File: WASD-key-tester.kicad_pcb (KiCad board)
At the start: 2 copper layers, 117 x 20 mm, 26 parts, among them J1 USB_B, J2 Conn_01x06, U1 ATTINY85-20SU

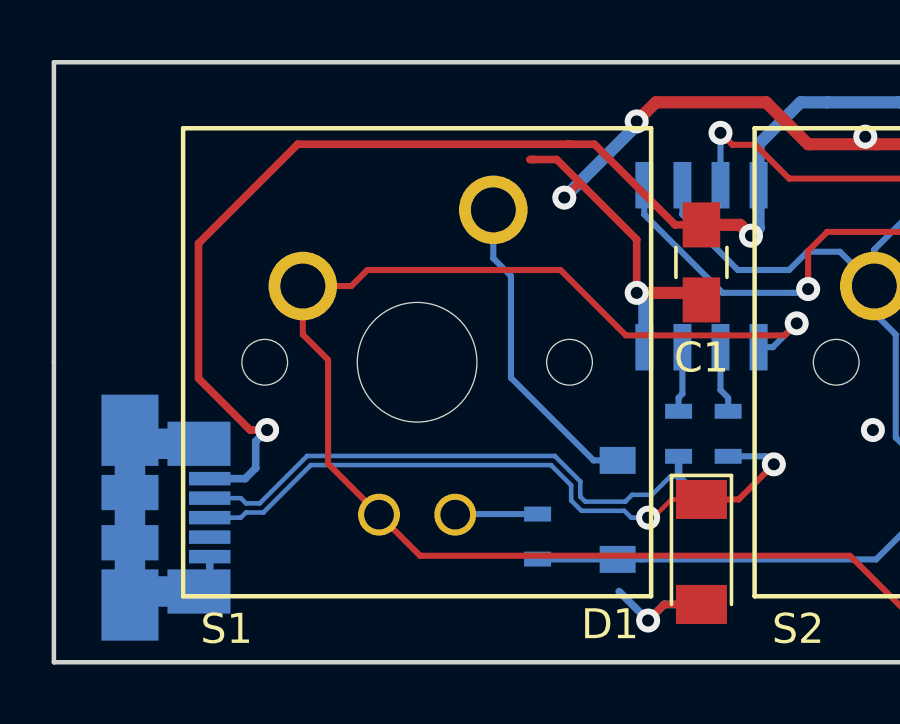
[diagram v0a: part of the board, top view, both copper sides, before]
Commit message: made power traces bigger beceause why not
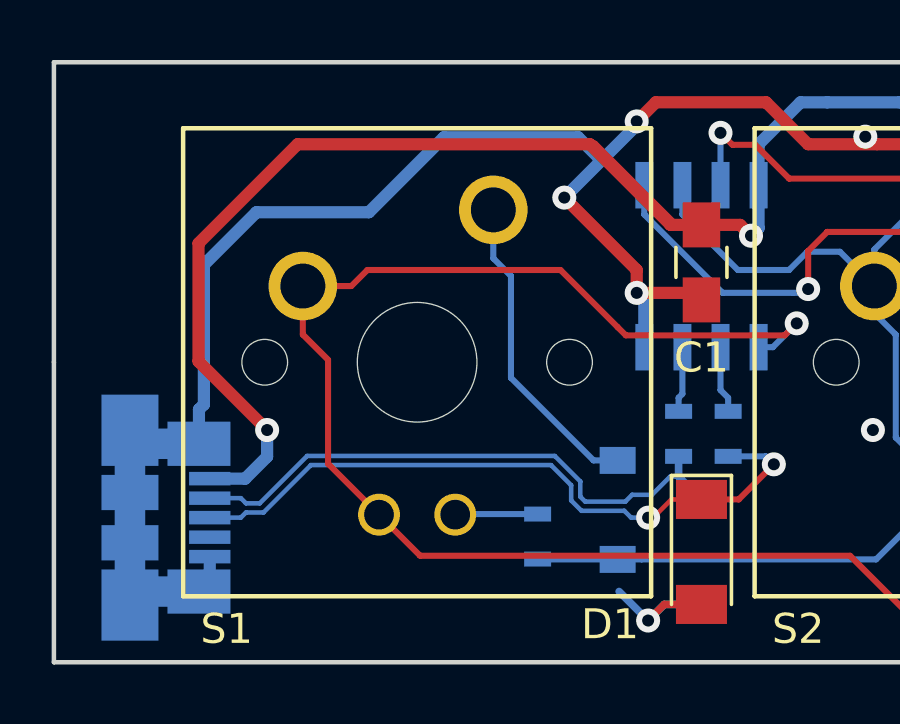
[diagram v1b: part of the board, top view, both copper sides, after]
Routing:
- net GND: track 74.1 -> 92.3 mm
- net +5V: track 75.6 -> 89.9 mm
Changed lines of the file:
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@@
     (thickness 1.6)
     (drawings 8)
-    (tracks 310)
+    (tracks 315)
     (zones 0)
     (modules 26)
@@
   )
   (setup
-    (last_trace_width 0.254)
+    (last_trace_width 0.4064)
     (user_trace_width 0.1524)
     (user_trace_width 0.2032)
@@
   (gr_line (start 214 175) (end 331 175) (layer Edge.Cuts) (width 0.15))
   (gr_line (start 214 165) (end 214 175) (layer Edge.Cuts) (width 0.15))
+  (segment (start 219.195 171.48) (end 219.195 172.2825) (width 0.4064) (layer Bottom) (net 1))
+  (segment (start 219.195 172.2825) (end 218.835 172.6425) (width 0.4064) (layer Bottom) (net 1))
+  (segment (start 233.426 162.687) (end 233.426 161.925) (width 0.4064) (layer Top) (net 1))
+  (segment (start 233.426 161.925) (end 231.013 159.512) (width 0.4064) (layer Top) (net 1))
+  (segment (start 233.426 157.099) (end 232.25 158.275) (width 0.4064) (layer Bottom) (net 1))
+  (segment (start 232.25 158.275) (end 231.013 159.512) (width 0.4064) (layer Bottom) (net 1))
+  (segment (start 227 157.5) (end 231.475 157.5) (width 0.4064) (layer Bottom) (net 1))
+  (segment (start 231.475 157.5) (end 232.25 158.275) (width 0.4064) (layer Bottom) (net 1))
+  (segment (start 224.5 160) (end 227 157.5) (width 0.4064) (layer Bottom) (net 1))
+  (segment (start 220.75 160) (end 224.5 160) (width 0.4064) (layer Bottom) (net 1))
+  (segment (start 219 161.75) (end 220.75 160) (width 0.4064) (layer Bottom) (net 1))
+  (segment (start 219 166.4086) (end 219 161.75) (width 0.4064) (layer Bottom) (net 1))
+  (segment (start 218.835 167.7175) (end 218.835 166.5736) (width 0.4064) (layer Bottom) (net 1))
+  (segment (start 218.835 166.5736) (end 219 166.4086) (width 0.4064) (layer Bottom) (net 1))
   (via (at 286.131 167.259) (size 0.8) (drill 0.4) (layers Top Bottom) (net 1))
   (via (at 278.257 168.148) (size 0.8) (drill 0.4) (layers Top Bottom) (net 1))
@@
   (via (at 241.3 167.259) (size 0.8) (drill 0.4) (layers Top Bottom) (net 1))
   (via (at 245.11 172.847) (size 0.8) (drill 0.4) (layers Top Bottom) (net 1))
-  (segment (start 230.759 158.242) (end 231.521 159.004) (width 0.254) (layer Top) (net 1))
-  (segment (start 231.521 159.004) (end 233.426 160.909) (width 0.254) (layer Top) (net 1))
-  (segment (start 231.013 159.512) (end 231.412999 159.112001) (width 0.254) (layer Top) (net 1))
-  (segment (start 231.412999 159.112001) (end 231.521 159.004) (width 0.254) (layer Top) (net 1))
   (segment (start 233.426 156.972) (end 233.426 157.099) (width 0.4064) (layer Bottom) (net 1))
-  (segment (start 233.426 157.099) (end 231.013 159.512) (width 0.4064) (layer Bottom) (net 1))
   (via (at 231.013 159.512) (size 0.8) (drill 0.4) (layers Top Bottom) (net 1))
   (segment (start 237.744 156.337) (end 234.061 156.337) (width 0.4064) (layer Top) (net 1))
@@
   (segment (start 272.0476 158.115) (end 272.5556 158.623) (width 0.4064) (layer Top) (net 1))
   (segment (start 244.475 158.115) (end 272.0476 158.115) (width 0.4064) (layer Top) (net 1))
-  (segment (start 233.426 160.909) (end 233.426 162.687) (width 0.254) (layer Top) (net 1))
-  (segment (start 229.87 158.242) (end 230.027 158.242) (width 0.254) (layer Top) (net 1))
-  (segment (start 229.87 158.242) (end 230.759 158.242) (width 0.254) (layer Top) (net 1))
   (segment (start 233.426 162.687) (end 235.351 162.687) (width 0.4064) (layer Top) (net 1))
   (segment (start 235.351 162.687) (end 235.585 162.921) (width 0.4064) (layer Top) (net 1))
@@
   (segment (start 234.343 173.073) (end 233.807 173.609) (width 0.254) (layer Bottom) (net 1))
   (via (at 233.807 173.609) (size 0.8) (drill 0.4) (layers Top Bottom) (net 1))
-  (segment (start 219.195 171.48) (end 219.195 172.2825) (width 0.254) (layer Bottom) (net 1))
-  (segment (start 219.195 172.2825) (end 218.835 172.6425) (width 0.254) (layer Bottom) (net 1))
   (segment (start 218.835 167.7175) (end 216.985 167.7175) (width 1.016) (layer Bottom) (net 1))
   (segment (start 216.985 167.7175) (end 216.535 167.2675) (width 1.016) (layer Bottom) (net 1))
@@
   (segment (start 218.835 172.6425) (end 216.985 172.6425) (width 1.016) (layer Bottom) (net 1))
   (segment (start 216.985 172.6425) (end 216.535 173.0925) (width 1.016) (layer Bottom) (net 1))
-  (segment (start 219.195 168.88) (end 220.375 168.88) (width 0.254) (layer Bottom) (net 2))
-  (segment (start 220.375 168.88) (end 220.726 168.529) (width 0.254) (layer Bottom) (net 2))
+  (segment (start 219.195 168.88) (end 220.375 168.88) (width 0.4064) (layer Bottom) (net 2))
+  (segment (start 220.375 168.88) (end 221.107 168.148) (width 0.4064) (layer Bottom) (net 2))
+  (segment (start 221.107 168.148) (end 221.107 167.259) (width 0.4064) (layer Bottom) (net 2))
+  (segment (start 237.49 159.098) (end 237.49 160.528) (width 0.4064) (layer Bottom) (net 2))
+  (segment (start 237.49 160.528) (end 237.236 160.782) (width 0.4064) (layer Bottom) (net 2))
+  (segment (start 218.821 161.036) (end 218.821 164.973) (width 0.4064) (layer Top) (net 2))
+  (segment (start 218.821 164.973) (end 221.107 167.259) (width 0.4064) (layer Top) (net 2))
+  (segment (start 222.123 157.734) (end 218.821 161.036) (width 0.4064) (layer Top) (net 2))
+  (segment (start 235.585 160.421) (end 234.5536 160.421) (width 0.4064) (layer Top) (net 2))
+  (segment (start 234.5536 160.421) (end 231.8666 157.734) (width 0.4064) (layer Top) (net 2))
+  (segment (start 231.8666 157.734) (end 222.123 157.734) (width 0.4064) (layer Top) (net 2))
   (segment (start 222.123 157.734) (end 231.14 157.734) (width 0.254) (layer Top) (net 2))
-  (segment (start 218.821 161.036) (end 222.123 157.734) (width 0.254) (layer Top) (net 2))
-  (segment (start 220.541315 167.259) (end 218.821 165.538685) (width 0.254) (layer Top) (net 2))
-  (segment (start 220.726 168.529) (end 220.726 167.64) (width 0.254) (layer Bottom) (net 2))
-  (segment (start 218.821 165.538685) (end 218.821 161.036) (width 0.254) (layer Top) (net 2))
   (via (at 221.107 167.259) (size 0.8) (drill 0.4) (layers Top Bottom) (net 2))
-  (segment (start 220.726 167.64) (end 221.107 167.259) (width 0.254) (layer Bottom) (net 2))
-  (segment (start 221.107 167.259) (end 220.541315 167.259) (width 0.254) (layer Top) (net 2))
   (segment (start 235.585 160.421) (end 236.875 160.421) (width 0.4064) (layer Top) (net 2))
   (segment (start 236.875 160.421) (end 237.236 160.782) (width 0.4064) (layer Top) (net 2))
-  (segment (start 237.49 159.098) (end 237.49 160.528) (width 0.4064) (layer Bottom) (net 2))
-  (segment (start 237.49 160.528) (end 237.236 160.782) (width 0.4064) (layer Bottom) (net 2))
   (via (at 237.236 160.782) (size 0.8) (drill 0.4) (layers Top Bottom) (net 2))
   (segment (start 238.887 156.337) (end 237.49 157.734) (width 0.4064) (layer Bottom) (net 2))
